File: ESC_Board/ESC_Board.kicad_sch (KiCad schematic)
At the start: 10 parts, among them Q1 BSC110N06NS3G, Q2 BSC110N06NS3G, U1 IR2103, U1 STM32F401RCTx

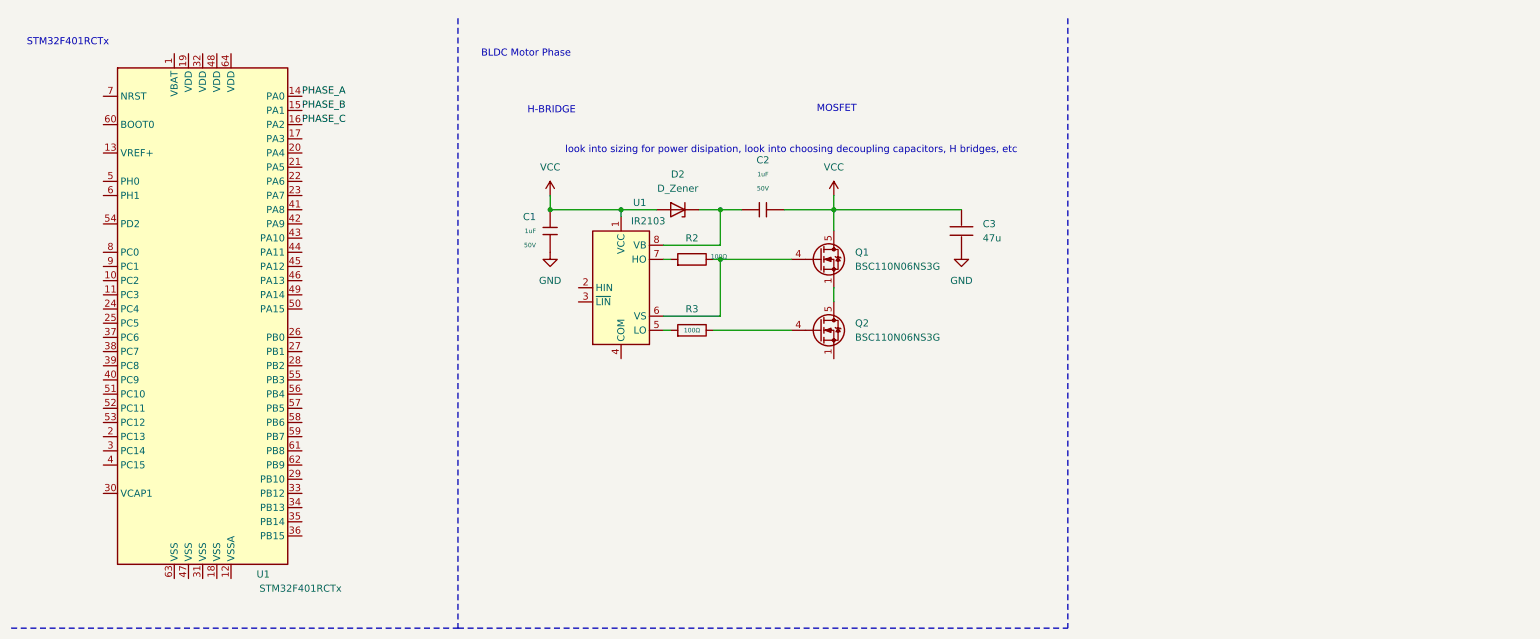
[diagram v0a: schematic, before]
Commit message: Changed MCU to be compatible with AM32, added Half Bridge driver and sensor circuitry
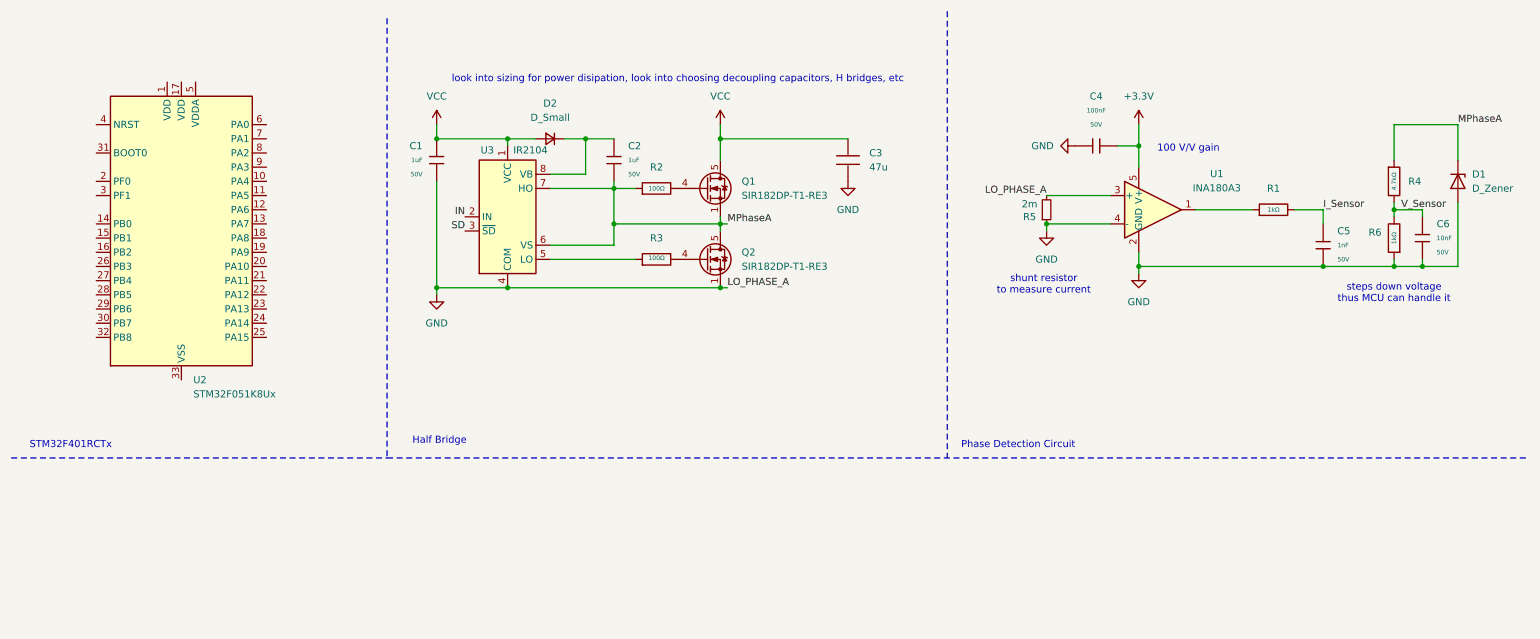
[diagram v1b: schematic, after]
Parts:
- removed D2: D_Zener, symbol Device:D_Zener
- removed U1: IR2103, Package_SO:SOIC-8-1EP_3.9x4.9mm_P1.27mm_EP2.29x3mm, symbol Driver_FET:IR2103
- removed U1: STM32F401RCTx, Package_QFP:LQFP-64_10x10mm_P0.5mm, symbol MCU_ST_STM32F4:STM32F401RCTx
- added C4: 100nF, PCM_JLCPCB:C_0402, symbol PCM_JLCPCB-Capacitors:0402,100nF,(2)
- added C5: 1nF, PCM_JLCPCB:C_0402, symbol PCM_JLCPCB-Capacitors:0402,1nF
- added C6: 10nF, PCM_JLCPCB:C_0603, symbol PCM_JLCPCB-Capacitors:0603,10nF
- added D1: D_Zener, symbol Device:D_Zener
- added D2: D_Small, symbol Device:D_Small
- added R1, R6: 1kΩ, PCM_JLCPCB:R_0402, symbol PCM_JLCPCB-Resistors:0402,1kΩ
- added R4: 4.7kΩ, PCM_JLCPCB:R_0402, symbol PCM_JLCPCB-Resistors:0402,4.7kΩ
- added R5: 2m, symbol Device:R_Small
- added U1: INA180A3, Package_TO_SOT_SMD:SOT-23-5, symbol Amplifier_Current:INA180A3
- added U2: STM32F051K8Ux, Package_DFN_QFN:QFN-32-1EP_5x5mm_P0.5mm_EP3.45x3.45mm, symbol MCU_ST_STM32F0:STM32F051K8Ux
- added U3: IR2104, symbol Driver_FET:IR2104
- Q1, Q2: value BSC110N06NS3G -> SIR182DP-T1-RE3
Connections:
- net GND: now also Q2.1 (S), Q2.2 (S), Q2.3 (S), C4.1, C5.2, C6.2, D1.2 (A), R5.1, R5.2, R6.1, U1.2 (GND), U1.3 (+), U1.4 (-), U3.4 (COM)
- net VCC: now also D2.2 (A), U3.1 (VCC); no longer C2.2
- net MPhaseA: now reaches Q1.1 (S), Q1.2 (S), Q1.3 (S), Q2.5 (D)
- net MPhaseA: now also C2.1, R2.1, D1.1 (K), R4.1, U3.6 (VS), U3.7 (HO)
- net at R3.1: now also U3.5 (LO)
- new net: C2.2, D2.1 (K), U3.8 (VB)
- new net: R1.1, U1.1
- new net +3.3V: C4.2, U1.5 (V+)
- new net IN: U3.2 (IN)
- new net I_Sensor: C5.1, R1.2
- new net SD: U3.3 (~{SD})
- new net V_Sensor: C6.1, R4.2, R6.2
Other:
- note added: "100 V/V gain"
- note added: "Half Bridge"
- note added: "Phase Detection Circuit"
- note added: "shunt resistor to measure current"
- note added: "steps down voltage thus MCU can handle it"
- note removed: "BLDC Motor Phase"
- note removed: "H-BRIDGE"
- note removed: "MOSFET"
- moved on the sheet: C1, C2, C3, Q1, Q2, R2, R3

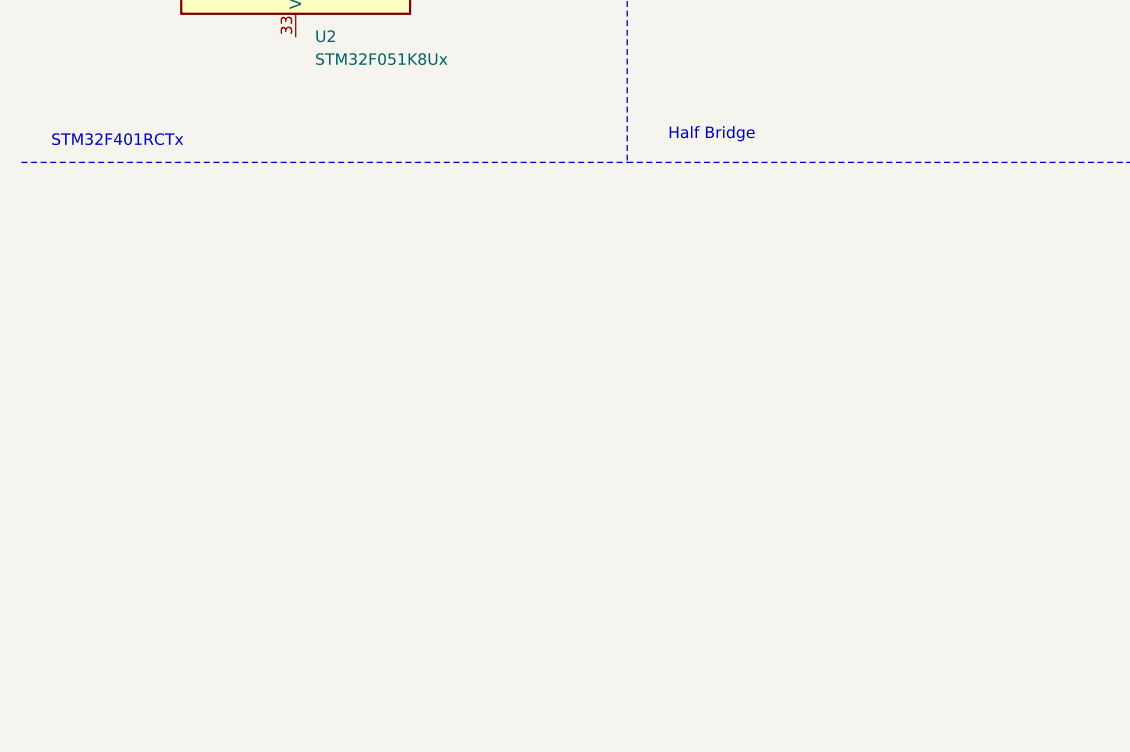
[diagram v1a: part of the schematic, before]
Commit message: Updated STM32 and overhauled SPI wiring, added external flash memory, added LoRa Transciever, moved buck converter to ESC-Board which will handle power distrubution, signficant progress on PCB design.
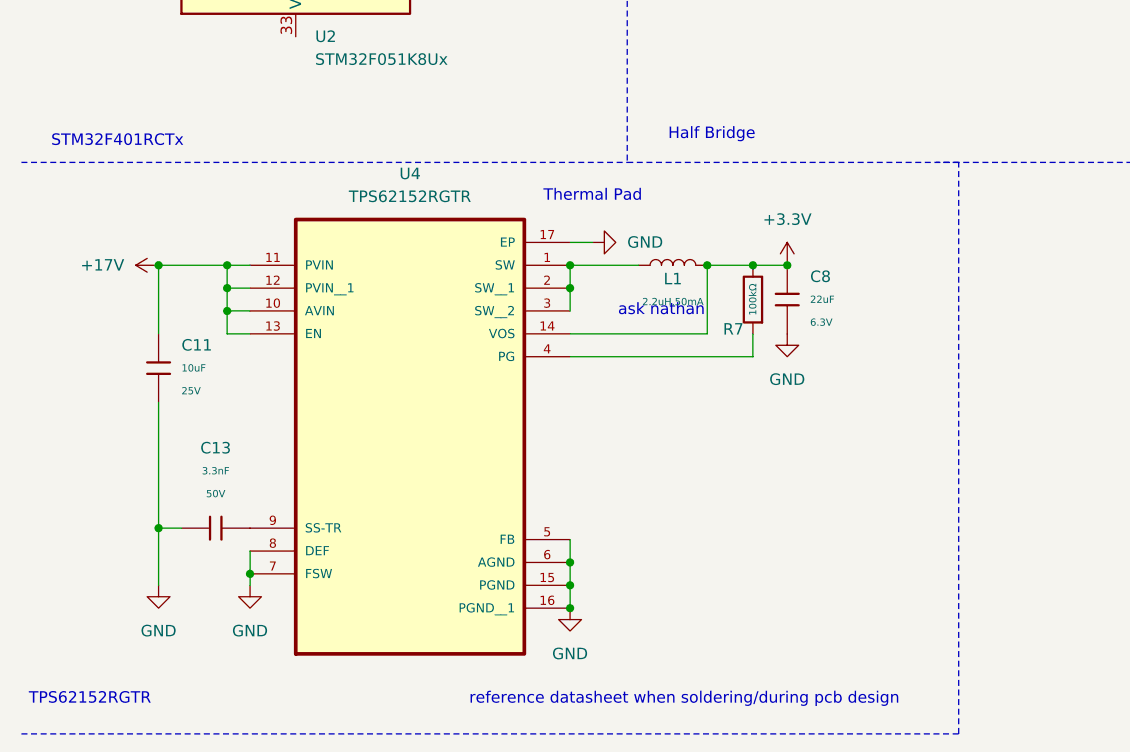
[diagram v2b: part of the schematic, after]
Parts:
- added C11: 10uF, PCM_JLCPCB:C_0603, symbol PCM_JLCPCB-Capacitors:0603,10uF,(2)
- added C13: 3.3nF, PCM_JLCPCB:C_0402, symbol PCM_JLCPCB-Capacitors:0402,3.3nF
- added C8: 22uF, PCM_JLCPCB:C_0603, symbol PCM_JLCPCB-Capacitors:0603,22uF
- added L1: 2.2uH,50mA, PCM_JLCPCB:L_0805, symbol PCM_JLCPCB-Inductors:2.2uH,50mA
- added R7: 100kΩ, PCM_JLCPCB:R_0402, symbol PCM_JLCPCB-Resistors:0402,100kΩ
- added U4: TPS62152RGTR, TPS62152RGTR:QFN50P300X300X100-17N, symbol TPS62152RGTR:TPS62152RGTR
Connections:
- net +3.3V: now also C8.1, L1.2, R7.2, U4.14 (VOS)
- net GND: now also C11.2, C13.1, C8.2, U4.15 (PGND), U4.16 (PGND__1), U4.17 (EP), U4.5 (FB), U4.6 (AGND), U4.7 (FSW), U4.8 (DEF)
- new net: R7.1, U4.4 (PG)
- new net: L1.1, U4.1 (SW), U4.2 (SW__1), U4.3 (SW__2)
- new net: C13.2, U4.9 (SS-TR)
- new net +17V: C11.1, U4.10 (AVIN), U4.11 (PVIN), U4.12 (PVIN__1), U4.13 (EN)
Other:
- note added: "TPS62152RGTR"
- note added: "Thermal Pad"
- note added: "ask nathan"
- note added: "reference datasheet when soldering/during pcb design"

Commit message: DroneController: Improved clarity of silkscreen and added manual reset test pad for the MCU.
ESC Board: Modified Buck Converter, added SWD debugging, added ICs for BLDC control
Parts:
- removed L1: 2.2uH,50mA, PCM_JLCPCB:L_0805, symbol PCM_JLCPCB-Inductors:2.2uH,50mA
- added C10: 4.7uF, PCM_JLCPCB:C_0402, symbol PCM_JLCPCB-Capacitors:0402,4.7uF
- added C12: 10nF, PCM_JLCPCB:C_0402, symbol PCM_JLCPCB-Capacitors:0402,10nF
- added C14: 1uF, PCM_JLCPCB:C_0402, symbol PCM_JLCPCB-Capacitors:0402,1uF
- added C15: 10uF, PCM_JLCPCB:C_0603, symbol PCM_JLCPCB-Capacitors:0603,10uF,(2)
- added C16, C17, C18, C19, C7, C9: 100nF, PCM_JLCPCB:C_0402, symbol PCM_JLCPCB-Capacitors:0402,100nF,(2)
- added L1: L, Inductor_SMD:L_1008_2520Metric, symbol Device:L
- added R10, R11, R12, R13, R14: 10kΩ, PCM_JLCPCB:R_0402, symbol PCM_JLCPCB-Resistors:0402,10kΩ
- added R8, R9: 22Ω, PCM_JLCPCB:R_0402, symbol PCM_JLCPCB-Resistors:0402,22Ω
- added TP1: TestPoint_2Pole, symbol Connector:TestPoint_2Pole
- added U5: DRV8300DRGER, RGE0024B-IPC_A, symbol 2025-07-10_00-49-41:DRV8300DRGER
- U4: value TPS62152RGTR -> TPS62153RGTT; footprint TPS62152RGTR:QFN50P300X300X100-17N -> Package_DFN_QFN:VQFN-16-1EP_3x3mm_P0.5mm_EP1.8x1.8mm; LCSC (none) -> C140300
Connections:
- net +3.3V: now also U2.1 (VDD), U2.17 (VDD), U2.5 (VDDA), C10.1, C12.1, C14.1, C7.1, C9.1, L1.2, R10.1
- net GND: now also U2.33 (VSS), C10.2, C12.2, C14.2, C16.2, C7.2, C9.2, R11.1, U5.25 (PowerPAD), U5.6 (GND)
- net at U4.1 (SW), U4.2 (SW__1), U4.3 (SW__2): now also L1.1
- net at U2.23 (PA13): now also R8.1
- net at U2.24 (PA14): now also R9.1
- net at U2.31 (BOOT0): now also R10.2, TP1.2
- net SWDR: now reaches U2.4 (NRST)
- net UART2_TX: now reaches U2.8 (PA2)
- net UART2_RX: now reaches U2.9 (PA3)
- new net: C19.2, U5.12 (SHC)
- new net: C19.1, U5.14 (BSTC)
- new net: C18.2, U5.15 (SHB)
- new net: C18.1, U5.17 (BSTB)
- new net: C17.2, U5.18 (SHA)
- new net: C17.1, U5.20 (BSTA)
- new net: R11.2, TP1.1
- new net +5V: C16.1, U5.4 (GVDD)
- new net SWCLK: R9.2
- new net SWDIO: R8.2
- no-connect marks 0 -> 5
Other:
- note added: "Really Good datasheet, esp on routing"
- note added: "integrated bootstrap diode"
- note added: "might reduce footprint of inductor"
- note removed: "ask nathan"
- moved on the sheet: C1, C2, C3, C4, C5, C6, D1, D2, Q1, Q2, R1, R2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

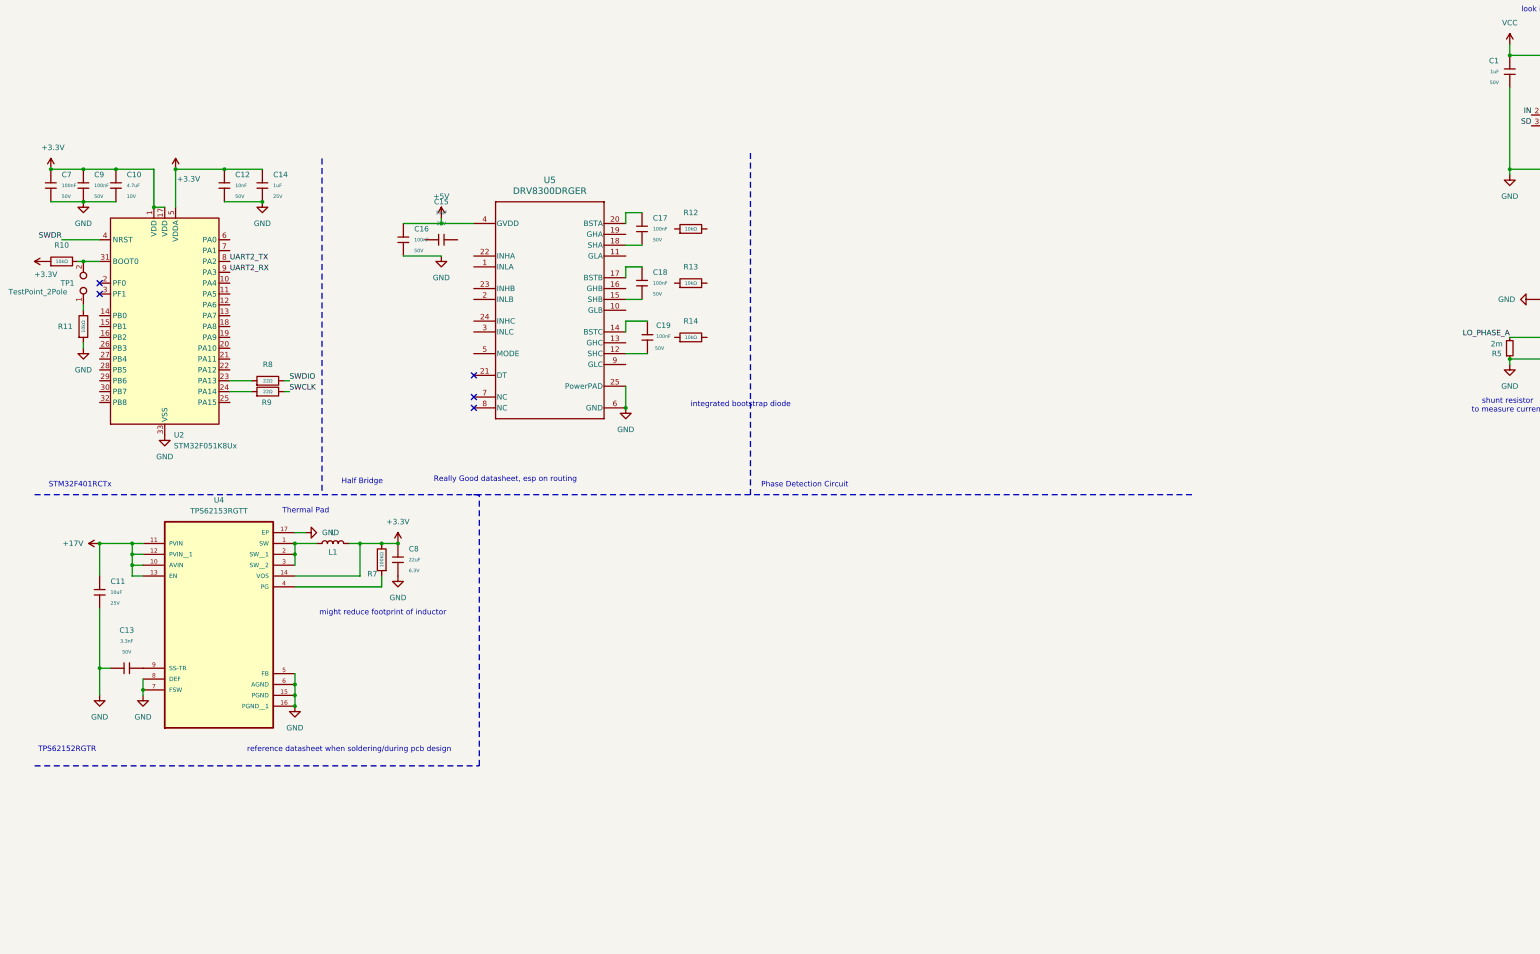
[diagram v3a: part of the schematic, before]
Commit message: ESC Board: added mosfets and BackEMF circuitry
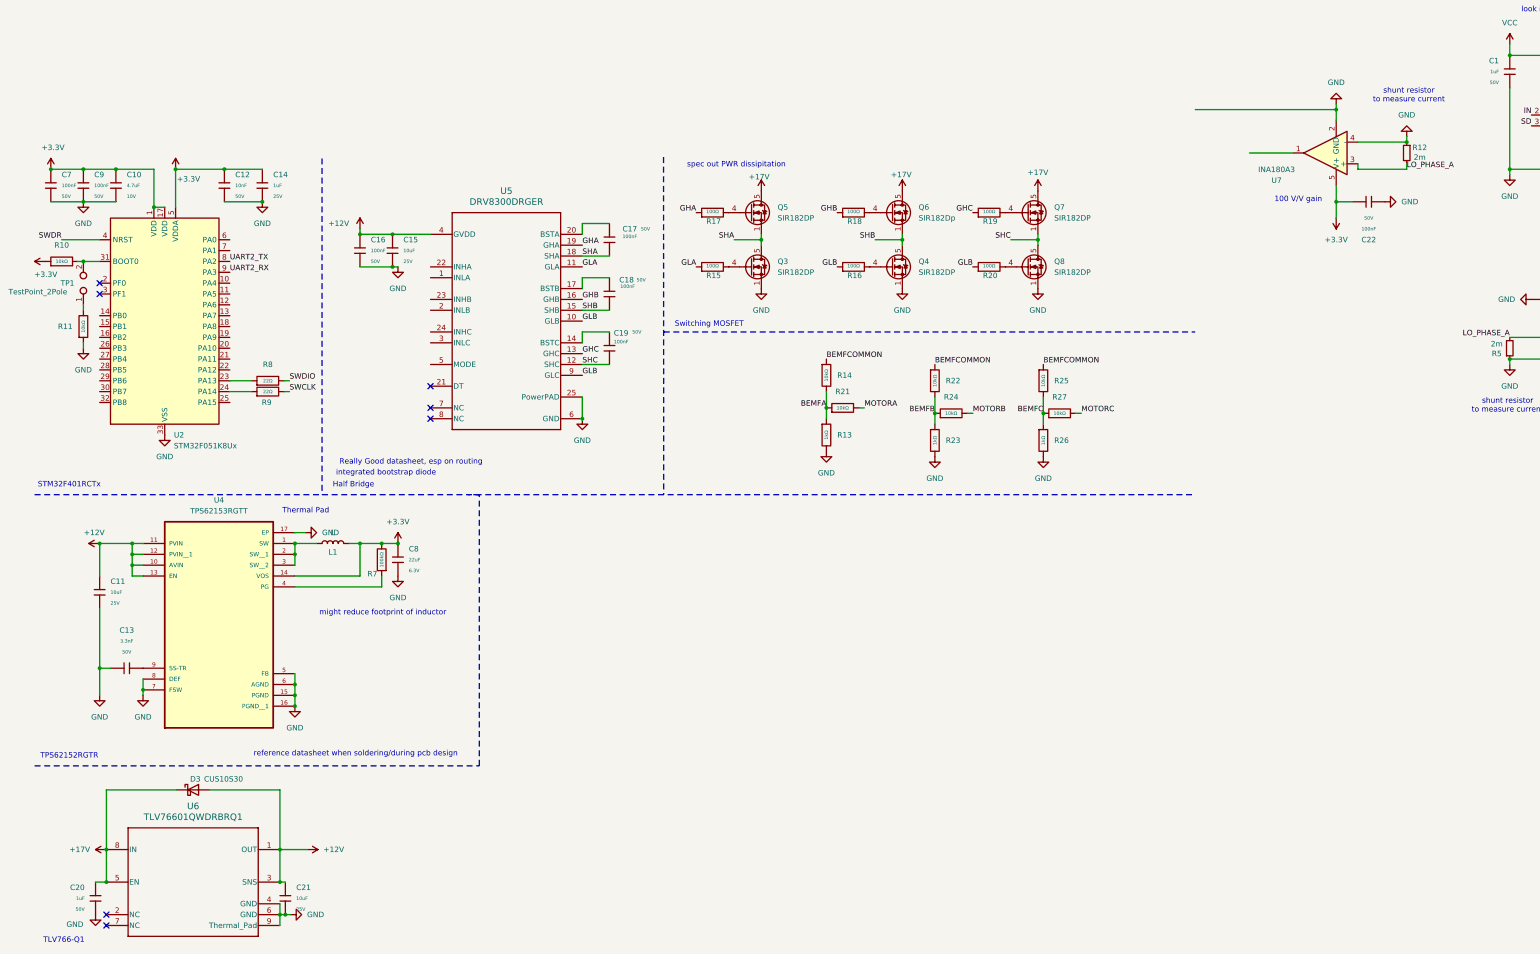
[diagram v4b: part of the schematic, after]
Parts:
- removed R12, R13, R14: 10kΩ, PCM_JLCPCB:R_0402, symbol PCM_JLCPCB-Resistors:0402,10kΩ
- added C20: 1uF, PCM_JLCPCB:C_0603, symbol PCM_JLCPCB-Capacitors:0603,1uF
- added C21: 10uF, PCM_JLCPCB:C_0603, symbol PCM_JLCPCB-Capacitors:0603,10uF,(2)
- added C22: 100nF, PCM_JLCPCB:C_0402, symbol PCM_JLCPCB-Capacitors:0402,100nF,(2)
- added D3: CUS10S30, symbol Device:D_Schottky
- added Q3, Q4, Q5, Q7, Q8: SIR182DP, Package_TO_SOT_SMD:TDSON-8-1, symbol Transistor_FET:BSC13DN30NSFD
- added Q6: SIR182Dp, Package_TO_SOT_SMD:TDSON-8-1, symbol Transistor_FET:BSC13DN30NSFD
- added R12: 2m, symbol Device:R_Small
- added R13, R23, R26: 1kΩ, PCM_JLCPCB:R_0603, symbol PCM_JLCPCB-Resistors:0603,1kΩ
- added R14, R21, R22, R24, R25, R27: 10kΩ, PCM_JLCPCB:R_0603, symbol PCM_JLCPCB-Resistors:0603,10kΩ
- added R15, R16, R17, R18, R19, R20: 100Ω, PCM_JLCPCB:R_0603, symbol PCM_JLCPCB-Resistors:0603,100Ω
- added U6: TLV76601QWDRBRQ1, DRB0008J-IPC_A, symbol TLV765501:TLV76601QWDRBRQ1
- added U7: INA180A3, Package_TO_SOT_SMD:SOT-23-5, symbol Amplifier_Current:INA180A3
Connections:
- net +5V is gone; now on net +12V: C16.1, U5.4 (GVDD)
- net +17V: now also C20.1, D3.1 (K), Q5.5 (D), Q6.5 (D), Q7.5 (D), U6.5 (EN), U6.8 (IN); no longer C11.1, U4.10 (AVIN), U4.11 (PVIN), U4.12 (PVIN__1), U4.13 (EN)
- net +3.3V: now also C22.2, U7.5 (V+)
- net GND: now also C15.1, C20.2, C21.2, C22.1, Q3.1 (S), Q3.2 (S), Q3.3 (S), Q4.1 (S), Q4.2 (S), Q4.3 (S), Q8.1 (S), Q8.2 (S), Q8.3 (S), R12.1, R12.2, R13.2, R23.2, R26.2, U6.4 (GND), U6.6 (GND), U6.9 (Thermal_Pad), U7.2 (GND), U7.3 (+), U7.4 (-)
- net GLB: now reaches U5.10 (GLB)
- net GLB: now also U5.9 (GLC), R16.1, R20.1
- net GLA: now reaches U5.11 (GLA)
- net GLA: now also R15.1
- net SHC: now reaches C19.2, U5.12 (SHC)
- net SHC: now also Q7.1 (S), Q7.2 (S), Q7.3 (S), Q8.5 (D)
- net GHC: now reaches U5.13 (GHC)
- net GHC: now also R19.1
- net SHB: now reaches C18.2, U5.15 (SHB)
- net SHB: now also Q4.5 (D), Q6.1 (S), Q6.2 (S), Q6.3 (S)
- net GHB: now reaches U5.16 (GHB)
- net GHB: now also R18.1
- net SHA: now reaches C17.2, U5.18 (SHA)
- net SHA: now also Q3.5 (D), Q5.1 (S), Q5.2 (S), Q5.3 (S)
- net GHA: now reaches U5.19 (GHA)
- net GHA: now also R17.1
- net +12V: now reaches C15.2
- net +12V: now also C11.1, U4.10 (AVIN), U4.11 (PVIN), U4.12 (PVIN__1), U4.13 (EN), C21.1, D3.2 (A), U6.1 (OUT), U6.3 (SNS)
- new net: Q4.4 (G), R16.2
- new net: Q8.4 (G), R20.2
- new net: Q6.4 (G), R18.2
- new net: Q5.4 (G), R17.2
- new net: Q7.4 (G), R19.2
- new net: Q3.4 (G), R15.2
- new net BEMFA: R13.1, R14.2, R21.1
- new net BEMFB: R22.2, R23.1, R24.1
- new net BEMFC: R25.2, R26.1, R27.1
- new net BEMFCOMMON: R14.1, R22.1, R25.1
- new net MOTORA: R21.2
- new net MOTORB: R24.2
- new net MOTORC: R27.2
- no-connect marks 5 -> 7
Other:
- note added: "Switching MOSFET"
- note added: "TLV766-Q1"
- note added: "spec out PWR dissipitation"
- note removed: "Phase Detection Circuit"
- moved on the sheet: C15, C16, C17, C18, C19, U5
